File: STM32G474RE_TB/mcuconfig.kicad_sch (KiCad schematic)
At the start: 9 parts, among them SW1 TS-1088-AR02016, Y1 ABM8G-24.000MHZ-18-D2Y-T

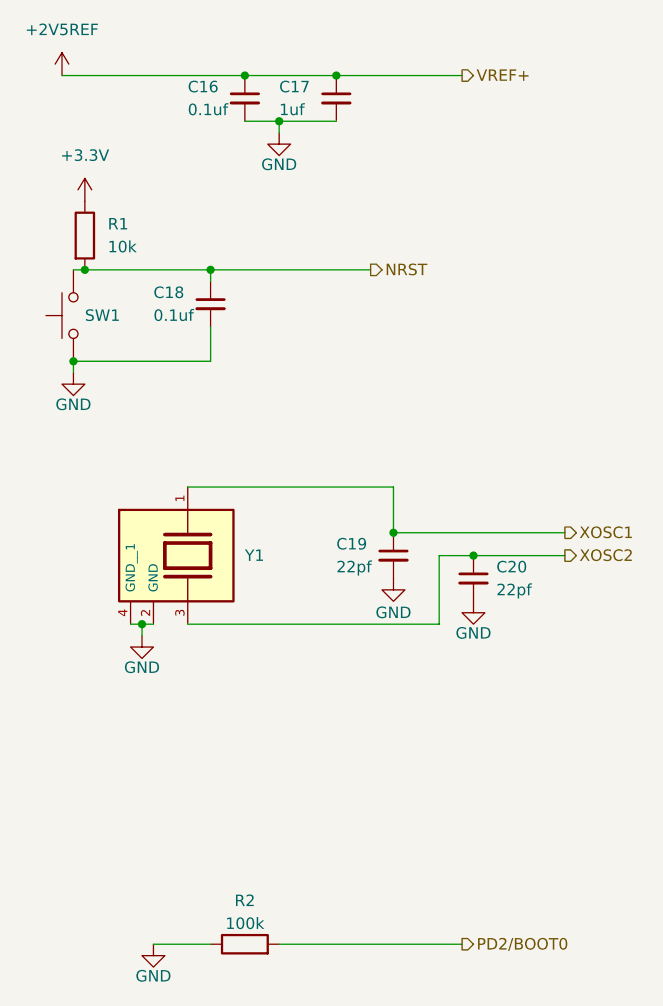
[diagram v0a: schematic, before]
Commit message: Added MOSFET template with led for debug or other functions
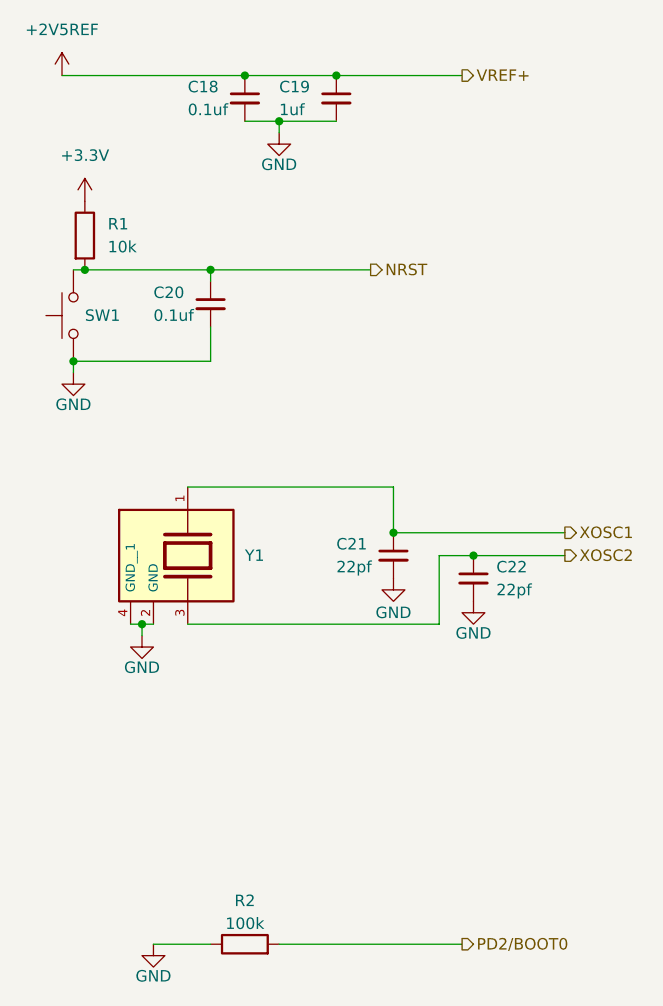
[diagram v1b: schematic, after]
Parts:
- renumbered C16 to C18, C17 to C19, C18 to C20, C19 to C21, C20 to C22
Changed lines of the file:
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@@
 		(on_board yes)
 		(dnp no)
-		(property "Reference" "C19"
+		(property "Reference" "C21"
 			(at 88.9 111.76 0)
 			(effects
@@
 			(project "STM32G474RE_TB"
 				(path "/c8ed293a-fe87-496b-9ed5-e9e5575d3b65/efbfa24d-5550-405a-8691-18f330b023b0"
-					(reference "C19")
+					(reference "C21")
 					(unit 1)
 				)
@@
 		(on_board yes)
 		(dnp no)
-		(property "Reference" "#PWR039"
+		(property "Reference" "#PWR042"
 			(at 82.55 72.39 0)
 			(effects
@@
 			(project "STM32G474RE_TB"
 				(path "/c8ed293a-fe87-496b-9ed5-e9e5575d3b65/efbfa24d-5550-405a-8691-18f330b023b0"
-					(reference "#PWR039")
+					(reference "#PWR042")
 					(unit 1)
 				)
@@
 		(on_board yes)
 		(dnp no)
-		(property "Reference" "#PWR041"
+		(property "Reference" "#PWR044"
 			(at 59.69 99.06 0)
 			(effects
@@
 			(project "STM32G474RE_TB"
 				(path "/c8ed293a-fe87-496b-9ed5-e9e5575d3b65/efbfa24d-5550-405a-8691-18f330b023b0"
-					(reference "#PWR041")
+					(reference "#PWR044")
 					(unit 1)
 				)
@@
 		(dnp no)
 		(fields_autoplaced yes)
-		(property "Reference" "#PWR040"
+		(property "Reference" "#PWR043"
 			(at 60.96 77.47 0)
 			(effects
@@
 			(project "STM32G474RE_TB"
 				(path "/c8ed293a-fe87-496b-9ed5-e9e5575d3b65/efbfa24d-5550-405a-8691-18f330b023b0"
-					(reference "#PWR040")
+					(reference "#PWR043")
 					(unit 1)
 				)
@@
 		(on_board yes)
 		(dnp no)
-		(property "Reference" "C18"
+		(property "Reference" "C20"
 			(at 68.58 83.82 0)
 			(effects
@@
 			(project "STM32G474RE_TB"
 				(path "/c8ed293a-fe87-496b-9ed5-e9e5575d3b65/efbfa24d-5550-405a-8691-18f330b023b0"
-					(reference "C18")
+					(reference "C20")
 					(unit 1)
 				)
@@
 		(on_board yes)
 		(dnp no)
-		(property "Reference" "#PWR044"
+		(property "Reference" "#PWR047"
 			(at 67.31 128.27 0)
 			(effects
@@
 			(project "STM32G474RE_TB"
 				(path "/c8ed293a-fe87-496b-9ed5-e9e5575d3b65/efbfa24d-5550-405a-8691-18f330b023b0"
-					(reference "#PWR044")
+					(reference "#PWR047")
 					(unit 1)
 				)
@@
 		(on_board yes)
 		(dnp no)
-		(property "Reference" "C17"
+		(property "Reference" "C19"
 			(at 82.55 60.96 0)
 			(effects
@@
 			(project "STM32G474RE_TB"
 				(path "/c8ed293a-fe87-496b-9ed5-e9e5575d3b65/efbfa24d-5550-405a-8691-18f330b023b0"
-					(reference "C17")
+					(reference "C19")
 					(unit 1)
 				)
@@
 		(on_board yes)
 		(dnp no)
-		(property "Reference" "#PWR045"
+		(property "Reference" "#PWR048"
 			(at 68.58 162.56 0)
 			(effects
@@
 			(project "STM32G474RE_TB"
 				(path "/c8ed293a-fe87-496b-9ed5-e9e5575d3b65/efbfa24d-5550-405a-8691-18f330b023b0"
-					(reference "#PWR045")
+					(reference "#PWR048")
 					(unit 1)
 				)
@@
 		(dnp no)
 		(fields_autoplaced yes)
-		(property "Reference" "#PWR038"
+		(property "Reference" "#PWR041"
 			(at 58.42 63.5 0)
 			(effects
@@
 			(project "STM32G474RE_TB"
 				(path "/c8ed293a-fe87-496b-9ed5-e9e5575d3b65/efbfa24d-5550-405a-8691-18f330b023b0"
-					(reference "#PWR038")
+					(reference "#PWR041")
 					(unit 1)
 				)
@@
 		(dnp no)
 		(fields_autoplaced yes)
-		(property "Reference" "C20"
+		(property "Reference" "C22"
 			(at 106.68 114.3062 0)
 			(effects
@@
 			(project "STM32G474RE_TB"
 				(path "/c8ed293a-fe87-496b-9ed5-e9e5575d3b65/efbfa24d-5550-405a-8691-18f330b023b0"
-					(reference "C20")
+					(reference "C22")
 					(unit 1)
 				)
@@
 		(on_board yes)
 		(dnp no)
-		(property "Reference" "#PWR042"
+		(property "Reference" "#PWR045"
 			(at 95.25 121.92 0)
 			(effects
@@
 			(project "STM32G474RE_TB"
 				(path "/c8ed293a-fe87-496b-9ed5-e9e5575d3b65/efbfa24d-5550-405a-8691-18f330b023b0"
-					(reference "#PWR042")
+					(reference "#PWR045")
 					(unit 1)
 				)
@@
 		(on_board yes)
 		(dnp no)
-		(property "Reference" "#PWR043"
+		(property "Reference" "#PWR046"
 			(at 104.14 124.46 0)
 			(effects
@@
 			(project "STM32G474RE_TB"
 				(path "/c8ed293a-fe87-496b-9ed5-e9e5575d3b65/efbfa24d-5550-405a-8691-18f330b023b0"
-					(reference "#PWR043")
+					(reference "#PWR046")
 					(unit 1)
 				)
@@
 		(on_board yes)
 		(dnp no)
-		(property "Reference" "C16"
+		(property "Reference" "C18"
 			(at 72.39 60.96 0)
 			(effects
@@
 			(project "STM32G474RE_TB"
 				(path "/c8ed293a-fe87-496b-9ed5-e9e5575d3b65/efbfa24d-5550-405a-8691-18f330b023b0"
-					(reference "C16")
-					(unit 1)
-				)
+					(reference "C18")
+					(unit 1)
+				)
